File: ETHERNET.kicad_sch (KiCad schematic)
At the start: 30 parts, among them Q1 S8050, U6 RTL8152B, Y2 25M

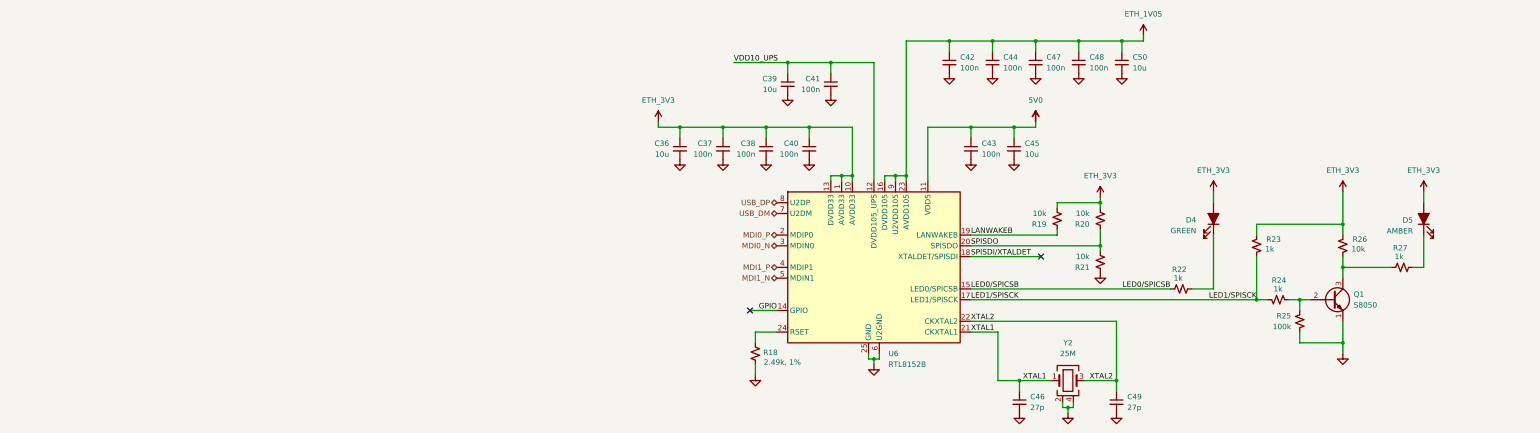
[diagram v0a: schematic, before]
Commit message: Schematic progress
I keep forgetting that I'm just making a panadapter here and not a full blown SDR...oops
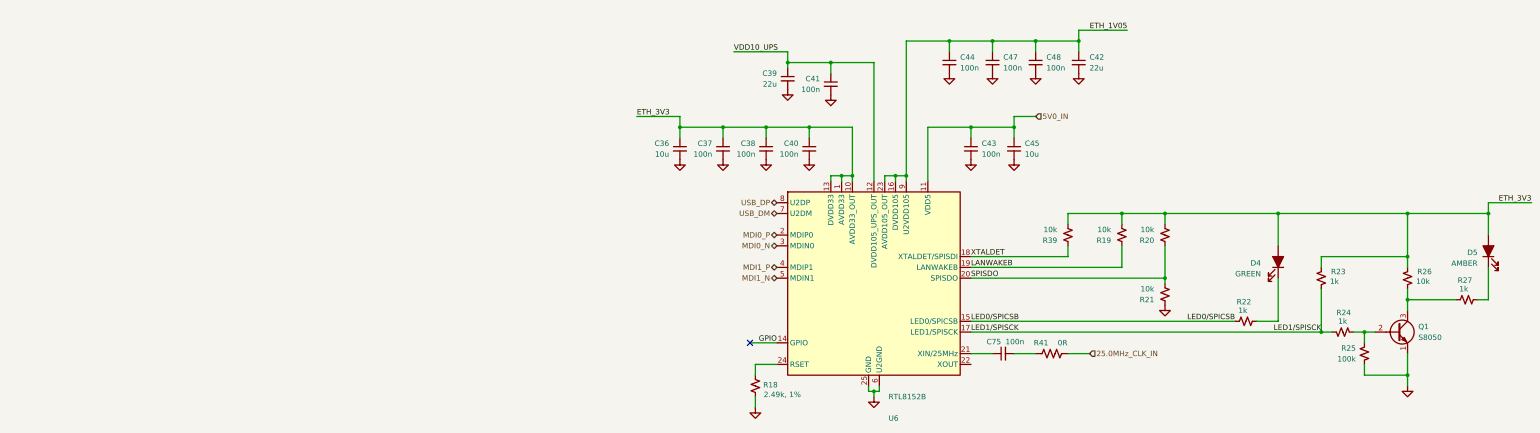
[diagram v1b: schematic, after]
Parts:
- removed C46, C49: 27p, libraries:Worthington_C_0402, symbol Device:C_Small
- removed C50: 10u, libraries:Worthington_C_0603, symbol Device:C_Small
- removed Y2: 25M, symbol Device:Crystal_GND24
- added C75: 100n, libraries:Worthington_C_0402, symbol Device:C_Small
- added R39: 10k, libraries:Worthington_R_0402, symbol Device:R_Small_US
- added R41: 0R, Resistor_SMD:R_0603_1608Metric_Pad0.98x0.95mm_HandSolder, symbol Device:R_US
- C39: value 10u -> 22u
- C42: value 100n -> 22u; footprint libraries:Worthington_C_0402 -> libraries:Worthington_C_0603
- R18, R19, R20, R21, R22, R23, R24, R25, R26, R27: footprint (none) -> libraries:Worthington_R_0402
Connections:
- net ETH_3V3: now also R39.2
- net 5V0 renamed 5V0_IN
- net SPISDI/XTALDET renamed XTALDET
- net XTALDET: now also R39.1
- net XTAL1: no longer names the net of U6.21 (XIN/25MHz)
- net XTAL1: now also C75.1
- net XTAL2: no longer names the net of U6.22 (XOUT)
- new net: C75.2, R41.1
- new net 25.0MHz_CLK_IN: R41.2
- no-connect marks 2 -> 1
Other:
- moved on the sheet: C44, C47, C48, D4, D5, Q1, R18, R19, R20, R21, R22, R23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

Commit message: Schematic progress
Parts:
- added C4: 1n, 2kV, Capacitor_SMD:C_1808_4520Metric, symbol Device:C_Small
- added C8, C9: 100n, libraries:Worthington_C_0402, symbol Device:C_Small
- added R56, R57, R59, R60: 75, libraries:Worthington_R_0402, symbol Device:R_Small_US
- added R58: 1M, libraries:Worthington_R_0402, symbol Device:R_Small_US
- added R61, R62: 10, libraries:Worthington_R_0402, symbol Device:R_Small_US
- added TR2: ALANL100X1-EF10ET, libraries:Transformer_Ethernet_ALAN100X1_SO-16_7.11x12.7mm, symbol Transformer:TG110-E050N5xx
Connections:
- net ETH_3V3: now also R61.2, R62.2
- net GND: now also C4.2, C8.2, C9.2, R58.1
- net MDI0_N: now also TR2.14 (TD+)
- net MDI0_P: now also TR2.16 (TD-)
- net MDI1_N: now also TR2.9 (RD+)
- net MDI1_P: now also TR2.11 (RD-)
- new net: C8.1, R61.1, TR2.10 (C_RD)
- new net: C9.1, R62.1, TR2.15 (C_TD)
- new net ETH_GND: C4.1, R56.2, R57.2, R58.2, R59.1, R60.1
- new net MCT0: R59.2, TR2.2 (C_TX)
- new net MCT1: R60.2, TR2.7 (C_RX)
- new net PJ1: TR2.1 (TX-)
- new net PJ2: TR2.3 (TX+)
- new net PJ3: TR2.6 (RX-)
- new net PJ4: R56.1
- new net PJ6: TR2.8 (RX+)
- new net PJ7: R57.1
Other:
- note added: "100-Ohm Differential Impedance"

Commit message: Schematic progress
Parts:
- removed C36, C45: 10u, libraries:Worthington_C_0603, symbol Device:C_Small
- removed C8, C9: 100n, libraries:Worthington_C_0402, symbol Device:C_Small
- removed R41: 0R, Resistor_SMD:R_0603_1608Metric_Pad0.98x0.95mm_HandSolder, symbol Device:R_US
- added C120, C121: 10u, libraries:Worthington_C_0402, symbol Device:C_Small
- added C69, C72: 100n, libraries:Worthington_C_0201, symbol Device:C_Small
- added R72: 1M, libraries:Worthington_R_0201, symbol Device:R_Small_US
- C37, C38, C40, C41, C43, C44, C47, C48, C75: footprint libraries:Worthington_C_0402 -> libraries:Worthington_C_0201; DigiKey (none) -> 445-15903-1-ND; Manufacturer Part Number (none) -> C0603X6S1C104K030BC; Voltage (none) -> 16V
- C4: value 1n, 2kV -> 1n, ±10%; Voltage (none) -> 2kV
- D4, D5: footprint (none) -> LED_SMD:LED_0402_1005Metric
- R18: value 2.49k, 1% -> 2.49k, ±1%; footprint libraries:Worthington_R_0402 -> libraries:Worthington_R_0201
- R19, R20, R21, R22, R23, R24, R25, R26, R27, R39, R61, R62: footprint libraries:Worthington_R_0402 -> libraries:Worthington_R_0201
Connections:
- net 25.0MHz_CLK_IN: now also C75.2
- net 5V0_IN: now also C47.1, C120.1; no longer C43.1
- net ETH_1V05: now also C43.1; no longer C47.1
- net ETH_3V3: now also C121.1
- net GND: now also C120.2, C121.2, C69.2, C72.2
- net at R61.1, TR2.10 (C_RD): now also C69.1
- net at C75.1, U6.21 (XIN/25MHz): now also R72.2
- net at U6.22 (XOUT): now also R72.1
- net at R62.1, TR2.15 (C_TD): now also C72.1

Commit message: Schematic and PCB progress
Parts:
- D5: renamed from D4; footprint LED_SMD:LED_0402_1005Metric -> libraries:Worthington_LED_0402
- D6: renamed from D5; footprint LED_SMD:LED_0402_1005Metric -> libraries:Worthington_LED_0402
- R25: renamed from R56; footprint libraries:Worthington_R_0402 -> libraries:Worthington_R_0201
- R26: renamed from R57; footprint libraries:Worthington_R_0402 -> libraries:Worthington_R_0201
- R27: renamed from R58; footprint libraries:Worthington_R_0402 -> libraries:Worthington_R_0201
- R28: renamed from R59; footprint libraries:Worthington_R_0402 -> libraries:Worthington_R_0201
- R29: renamed from R60; footprint libraries:Worthington_R_0402 -> libraries:Worthington_R_0201
- renumbered C4 to C34, C69 to C35, C72 to C36, C121 to C37, C37 to C38, C38 to C39, C39 to C40, C40 to C41, C41 to C42, C47 to C44, C44 to C45, C120 to C46, C48 to C47, C75 to C48, C42 to C49, R61 to R30, R62 to R31, R18 to R32, R72 to R33, R39 to R34, R19 to R35, R20 to R36, R21 to R37, R22 to R38, R23 to R39, R24 to R40, R25 to R41, R26 to R42, R27 to R43, TR2 to TR1, U6 to U8

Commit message: PCB and schematic progress
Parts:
- C40, C49: value 22u -> 10u; footprint libraries:Worthington_C_0603 -> libraries:Worthington_C_0402; DigiKey (none) -> 4713-GMC04X5R106M10NTCT-ND; Manufacturer Part Number (none) -> GMC04X5R106M10NT; Voltage (none) -> 10V

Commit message: PCB and schematic progress
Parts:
- Q1: value S8050 -> S8050T; footprint Package_TO_SOT_SMD:SOT-23 -> Package_TO_SOT_SMD:SOT-523; DigiKey (none) -> 6557-S8050TTR-ND
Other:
- moved on the sheet: C34, R25, R26, R27, R28, R29
